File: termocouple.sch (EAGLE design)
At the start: 19 parts, among them IC1 MAX6675, IC2 MAX6675, IC3 MAX6675, IC4 MAX6675, U2 TC1262_VDB, X2 1751248, X3 1751248, X4 1751248, X5 1751248

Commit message: sch update
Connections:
- removed net 3V3: C4.1, U2.VOUT
- net +3V3: now also C4.1, U2.VOUT; no longer U$1.3.3V, U$1.3V3
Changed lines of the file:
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@@
 <part name="IC4" library="adafruit" deviceset="MAX6675" device=""/>
 <part name="+3V1" library="supply1" deviceset="+3V3" device=""/>
-<part name="+3V2" library="supply1" deviceset="+3V3" device=""/>
-<part name="+3V3" library="supply1" deviceset="+3V3" device=""/>
 <part name="GND1" library="supply1" deviceset="GND" device=""/>
 <part name="GND2" library="supply1" deviceset="GND" device=""/>
@@
 <part name="X4" library="con-phoenix-350" deviceset="1751248" device=""/>
 <part name="X5" library="con-phoenix-350" deviceset="1751248" device=""/>
+<part name="+3V6" library="supply1" deviceset="+3V3" device=""/>
 </parts>
 <sheets>
@@
 <instance part="IC4" gate="G$1" x="-5.08" y="22.86"/>
 <instance part="+3V1" gate="G$1" x="-25.4" y="78.74" rot="R90"/>
-<instance part="+3V2" gate="G$1" x="55.88" y="45.72" rot="R90"/>
-<instance part="+3V3" gate="G$1" x="99.06" y="58.42"/>
 <instance part="GND1" gate="1" x="86.36" y="81.28"/>
 <instance part="GND2" gate="1" x="-20.32" y="71.12" rot="R270"/>
@@
 <instance part="X5" gate="-1" x="-45.72" y="15.24" rot="R180"/>
 <instance part="X5" gate="-2" x="-45.72" y="25.4" rot="R180"/>
+<instance part="+3V6" gate="G$1" x="142.24" y="101.6"/>
 </instances>
 <busses>
@@
 </segment>
 <segment>
-<pinref part="U$1" gate="G$1" pin="3.3V"/>
-<pinref part="+3V2" gate="G$1" pin="+3V3"/>
-</segment>
-<segment>
-<pinref part="U$1" gate="G$1" pin="3V3"/>
-<pinref part="+3V3" gate="G$1" pin="+3V3"/>
-</segment>
-<segment>
 <pinref part="X1" gate="-1" pin="1"/>
 <pinref part="+3V4" gate="G$1" pin="+3V3"/>
+</segment>
+<segment>
+<pinref part="U2" gate="U1" pin="VOUT"/>
+<label x="139.7" y="101.6" size="1.778" layer="95"/>
+<pinref part="C4" gate="G$1" pin="1"/>
+<wire x1="137.16" y1="99.06" x2="142.24" y2="99.06" width="0.1524" layer="91"/>
+<wire x1="142.24" y1="99.06" x2="142.24" y2="96.52" width="0.1524" layer="91"/>
+<pinref part="+3V6" gate="G$1" pin="+3V3"/>
+<junction x="142.24" y="99.06"/>
 </segment>
 </net>
@@
 </segment>
 </net>
-<net name="3V3" class="0">
-<segment>
-<pinref part="U2" gate="U1" pin="VOUT"/>
-<label x="139.7" y="101.6" size="1.778" layer="95"/>
-<pinref part="C4" gate="G$1" pin="1"/>
-<wire x1="137.16" y1="99.06" x2="142.24" y2="99.06" width="0.1524" layer="91"/>
-<wire x1="142.24" y1="99.06" x2="142.24" y2="96.52" width="0.1524" layer="91"/>
-</segment>
-</net>

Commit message: pcb
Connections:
- net N$2: now also IC1.SCK
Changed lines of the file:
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@@
 <wire x1="104.14" y1="5.08" x2="20.32" y2="5.08" width="0.1524" layer="91"/>
 <wire x1="20.32" y1="5.08" x2="20.32" y2="20.32" width="0.1524" layer="91"/>
+<junction x="20.32" y="20.32"/>
 </segment>
 </net>
@@
 <wire x1="17.78" y1="38.1" x2="17.78" y2="60.96" width="0.1524" layer="91"/>
 <wire x1="17.78" y1="60.96" x2="17.78" y2="83.82" width="0.1524" layer="91"/>
-<wire x1="17.78" y1="83.82" x2="7.62" y2="83.82" width="0.1524" layer="91"/>
 <pinref part="IC3" gate="G$1" pin="SCK"/>
 <wire x1="10.16" y1="38.1" x2="17.78" y2="38.1" width="0.1524" layer="91"/>
@@
 <pinref part="U$1" gate="G$1" pin="D4"/>
 <wire x1="99.06" y1="25.4" x2="106.68" y2="25.4" width="0.1524" layer="91"/>
+<junction x="17.78" y="15.24"/>
+<pinref part="IC1" gate="G$1" pin="SCK"/>
+<wire x1="10.16" y1="83.82" x2="17.78" y2="83.82" width="0.1524" layer="91"/>
 </segment>
 </net>

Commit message: wiring change
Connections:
- removed net N$11: U$1.D11, X1-6.1
- removed net N$12: U$1.D12, X1-5.1
- new net N$24: X1-6.1
- new net N$25: X1-5.1
- net N$1: now also U$1.D7; no longer U$1.D3
- net N$10: no longer U$1.D10
- net N$2: now also U$1.D8; no longer U$1.D4
- net N$3: now also U$1.D10; no longer U$1.D6
- net N$4: now also U$1.D9; no longer U$1.D5
- net N$6: now also U$1.D11; no longer U$1.D7
- net N$7: now also U$1.D12; no longer U$1.D8
- net N$9: no longer U$1.D9
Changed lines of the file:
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@@
 <junction x="20.32" y="66.04"/>
 <junction x="20.32" y="43.18"/>
-<pinref part="U$1" gate="G$1" pin="D3"/>
-<wire x1="99.06" y1="22.86" x2="104.14" y2="22.86" width="0.1524" layer="91"/>
-<wire x1="104.14" y1="22.86" x2="104.14" y2="5.08" width="0.1524" layer="91"/>
+<wire x1="104.14" y1="33.02" x2="104.14" y2="5.08" width="0.1524" layer="91"/>
 <wire x1="104.14" y1="5.08" x2="20.32" y2="5.08" width="0.1524" layer="91"/>
 <wire x1="20.32" y1="5.08" x2="20.32" y2="20.32" width="0.1524" layer="91"/>
 <junction x="20.32" y="20.32"/>
+<pinref part="U$1" gate="G$1" pin="D7"/>
+<wire x1="99.06" y1="33.02" x2="104.14" y2="33.02" width="0.1524" layer="91"/>
 </segment>
 </net>
@@
 <wire x1="17.78" y1="15.24" x2="17.78" y2="2.54" width="0.1524" layer="91"/>
 <wire x1="17.78" y1="2.54" x2="106.68" y2="2.54" width="0.1524" layer="91"/>
-<wire x1="106.68" y1="2.54" x2="106.68" y2="25.4" width="0.1524" layer="91"/>
-<pinref part="U$1" gate="G$1" pin="D4"/>
-<wire x1="99.06" y1="25.4" x2="106.68" y2="25.4" width="0.1524" layer="91"/>
+<wire x1="106.68" y1="2.54" x2="106.68" y2="35.56" width="0.1524" layer="91"/>
 <junction x="17.78" y="15.24"/>
 <pinref part="IC1" gate="G$1" pin="SCK"/>
 <wire x1="10.16" y1="83.82" x2="17.78" y2="83.82" width="0.1524" layer="91"/>
+<pinref part="U$1" gate="G$1" pin="D8"/>
+<wire x1="99.06" y1="35.56" x2="106.68" y2="35.56" width="0.1524" layer="91"/>
 </segment>
 </net>
@@
 <wire x1="22.86" y1="86.36" x2="22.86" y2="0" width="0.1524" layer="91"/>
 <wire x1="22.86" y1="0" x2="109.22" y2="0" width="0.1524" layer="91"/>
-<wire x1="109.22" y1="0" x2="109.22" y2="27.94" width="0.1524" layer="91"/>
-<pinref part="U$1" gate="G$1" pin="D5"/>
-<wire x1="109.22" y1="27.94" x2="99.06" y2="27.94" width="0.1524" layer="91"/>
+<wire x1="109.22" y1="0" x2="109.22" y2="38.1" width="0.1524" layer="91"/>
+<pinref part="U$1" gate="G$1" pin="D9"/>
+<wire x1="99.06" y1="38.1" x2="109.22" y2="38.1" width="0.1524" layer="91"/>
 </segment>
 </net>
@@
 <pinref part="IC3" gate="G$1" pin="/CS"/>
 <wire x1="10.16" y1="40.64" x2="27.94" y2="40.64" width="0.1524" layer="91"/>
-<pinref part="U$1" gate="G$1" pin="D7"/>
-<wire x1="99.06" y1="33.02" x2="114.3" y2="33.02" width="0.1524" layer="91"/>
-<wire x1="114.3" y1="33.02" x2="114.3" y2="-5.08" width="0.1524" layer="91"/>
+<wire x1="114.3" y1="43.18" x2="114.3" y2="-5.08" width="0.1524" layer="91"/>
 <wire x1="114.3" y1="-5.08" x2="27.94" y2="-5.08" width="0.1524" layer="91"/>
 <wire x1="27.94" y1="-5.08" x2="27.94" y2="40.64" width="0.1524" layer="91"/>
-</segment>
-</net>
-<net name="N$3" class="0">
-<segment>
-<pinref part="IC2" gate="G$1" pin="/CS"/>
-<wire x1="10.16" y1="63.5" x2="25.4" y2="63.5" width="0.1524" layer="91"/>
-<wire x1="25.4" y1="63.5" x2="25.4" y2="-2.54" width="0.1524" layer="91"/>
-<pinref part="U$1" gate="G$1" pin="D6"/>
-<wire x1="111.76" y1="30.48" x2="99.06" y2="30.48" width="0.1524" layer="91"/>
-<wire x1="25.4" y1="-2.54" x2="111.76" y2="-2.54" width="0.1524" layer="91"/>
-<wire x1="111.76" y1="-2.54" x2="111.76" y2="30.48" width="0.1524" layer="91"/>
+<pinref part="U$1" gate="G$1" pin="D11"/>
+<wire x1="99.06" y1="43.18" x2="114.3" y2="43.18" width="0.1524" layer="91"/>
 </segment>
 </net>
@@
 <wire x1="15.24" y1="17.78" x2="15.24" y2="-7.62" width="0.1524" layer="91"/>
 <wire x1="15.24" y1="-7.62" x2="116.84" y2="-7.62" width="0.1524" layer="91"/>
-<wire x1="116.84" y1="-7.62" x2="116.84" y2="35.56" width="0.1524" layer="91"/>
-<pinref part="U$1" gate="G$1" pin="D8"/>
-<wire x1="116.84" y1="35.56" x2="99.06" y2="35.56" width="0.1524" layer="91"/>
+<wire x1="116.84" y1="-7.62" x2="116.84" y2="45.72" width="0.1524" layer="91"/>
+<pinref part="U$1" gate="G$1" pin="D12"/>
+<wire x1="116.84" y1="45.72" x2="99.06" y2="45.72" width="0.1524" layer="91"/>
 </segment>
 </net>
@@
 <net name="N$9" class="0">
 <segment>
-<pinref part="U$1" gate="G$1" pin="D9"/>
-<wire x1="99.06" y1="38.1" x2="121.92" y2="38.1" width="0.1524" layer="91"/>
-<wire x1="121.92" y1="38.1" x2="121.92" y2="27.94" width="0.1524" layer="91"/>
 <pinref part="X1" gate="-8" pin="1"/>
 <wire x1="121.92" y1="27.94" x2="152.4" y2="27.94" width="0.1524" layer="91"/>
@@
 <net name="N$10" class="0">
 <segment>
-<pinref part="U$1" gate="G$1" pin="D10"/>
-<wire x1="99.06" y1="40.64" x2="124.46" y2="40.64" width="0.1524" layer="91"/>
-<wire x1="124.46" y1="40.64" x2="124.46" y2="33.02" width="0.1524" layer="91"/>
 <pinref part="X1" gate="-7" pin="1"/>
 <wire x1="124.46" y1="33.02" x2="152.4" y2="33.02" width="0.1524" layer="91"/>
-</segment>
-</net>
-<net name="N$11" class="0">
-<segment>
-<pinref part="U$1" gate="G$1" pin="D11"/>
-<wire x1="99.06" y1="43.18" x2="127" y2="43.18" width="0.1524" layer="91"/>
-<wire x1="127" y1="43.18" x2="127" y2="38.1" width="0.1524" layer="91"/>
-<pinref part="X1" gate="-6" pin="1"/>
-<wire x1="127" y1="38.1" x2="152.4" y2="38.1" width="0.1524" layer="91"/>
-</segment>
-</net>
-<net name="N$12" class="0">
-<segment>
-<pinref part="U$1" gate="G$1" pin="D12"/>
-<wire x1="99.06" y1="45.72" x2="129.54" y2="45.72" width="0.1524" layer="91"/>
-<wire x1="129.54" y1="45.72" x2="129.54" y2="43.18" width="0.1524" layer="91"/>
-<pinref part="X1" gate="-5" pin="1"/>
-<wire x1="129.54" y1="43.18" x2="152.4" y2="43.18" width="0.1524" layer="91"/>
 </segment>
 </net>
@@
 </segment>
 </net>
+<net name="N$24" class="0">
+<segment>
+<pinref part="X1" gate="-6" pin="1"/>
+<wire x1="127" y1="38.1" x2="152.4" y2="38.1" width="0.1524" layer="91"/>
+</segment>
+</net>
+<net name="N$25" class="0">
+<segment>
+<pinref part="X1" gate="-5" pin="1"/>
+<wire x1="129.54" y1="43.18" x2="152.4" y2="43.18" width="0.1524" layer="91"/>
+</segment>
+</net>
+<net name="N$3" class="0">
+<segment>
+<pinref part="U$1" gate="G$1" pin="D10"/>
+<wire x1="99.06" y1="40.64" x2="111.76" y2="40.64" width="0.1524" layer="91"/>
+<pinref part="IC2" gate="G$1" pin="/CS"/>
+<wire x1="10.16" y1="63.5" x2="25.4" y2="63.5" width="0.1524" layer="91"/>
+<wire x1="25.4" y1="63.5" x2="25.4" y2="-2.54" width="0.1524" layer="91"/>
+<wire x1="25.4" y1="-2.54" x2="111.76" y2="-2.54" width="0.1524" layer="91"/>
+<wire x1="111.76" y1="-2.54" x2="111.76" y2="40.64" width="0.1524" layer="91"/>
+</segment>
+</net>

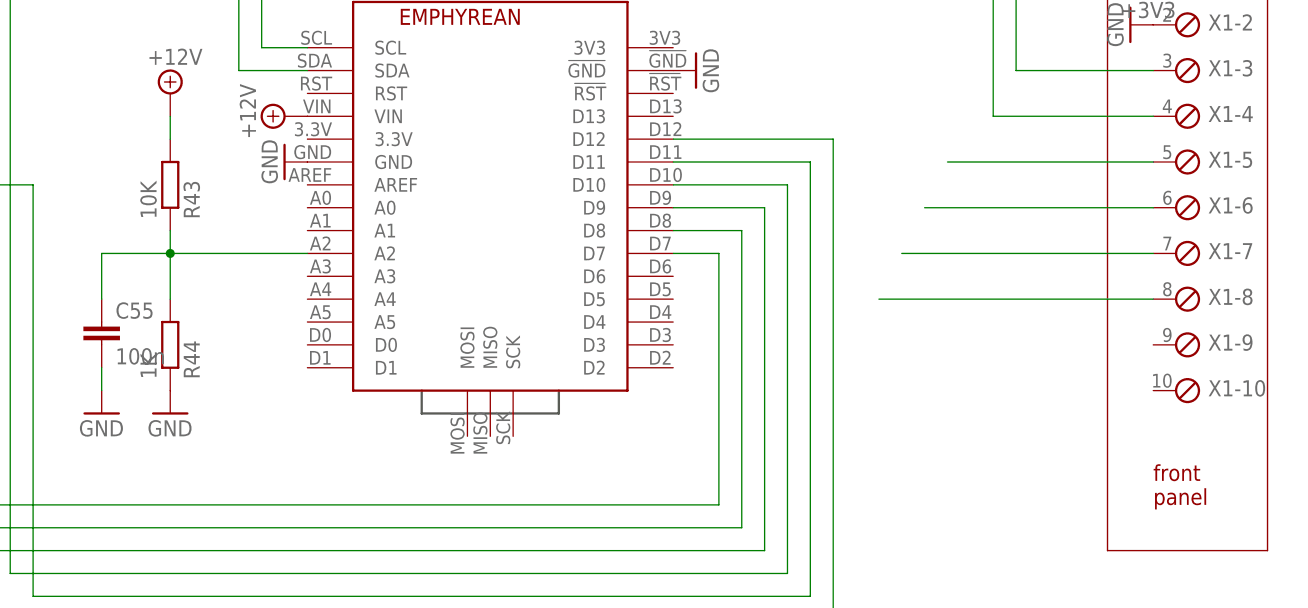
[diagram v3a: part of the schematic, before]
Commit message: front panel + brd traces
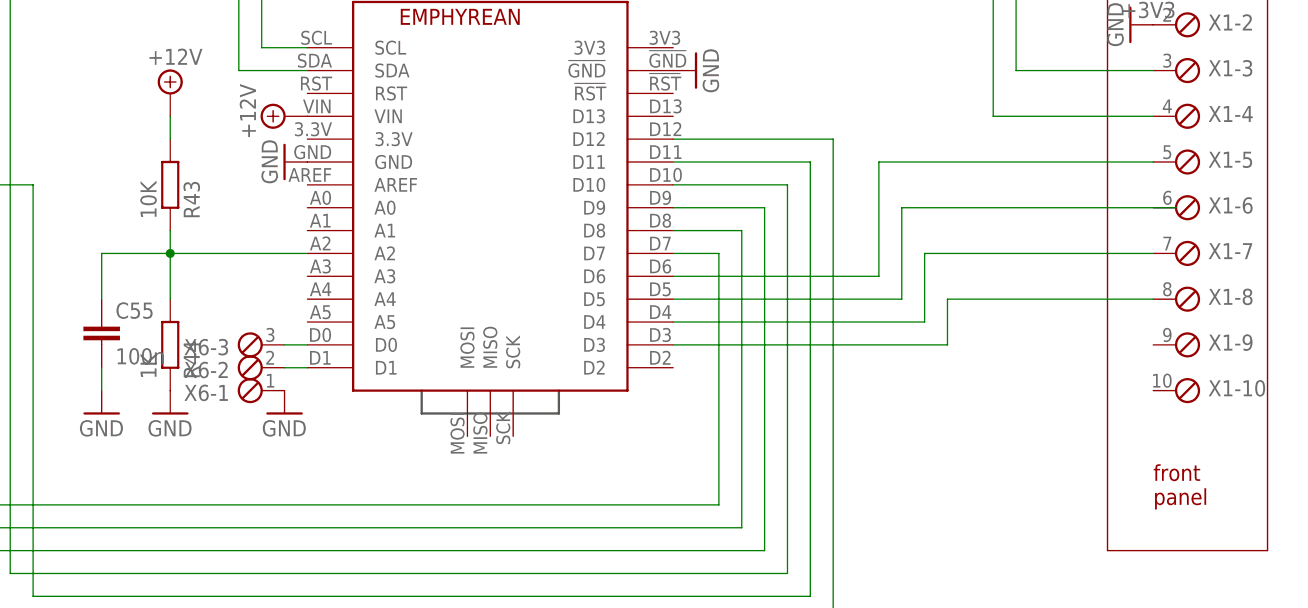
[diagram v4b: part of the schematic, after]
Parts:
- added X6: (no value), con-phoenix-254:MPT3
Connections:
- removed net N$24: X1-6.1
- removed net N$25: X1-5.1
- new net N$11: U$1.D4, X1-7.1
- new net N$12: U$1.D3, X1-8.1
- new net N$22: U$1.D0, X6-3.1
- new net N$23: U$1.D1, X6-2.1
- net GND: now also X6-1.1
- net N$10: now also U$1.D5; no longer X1-7.1
- net N$9: now also U$1.D6, X1-5.1; no longer X1-8.1
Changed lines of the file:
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@@
 <part name="X5" library="con-phoenix-350" deviceset="1751248" device=""/>
 <part name="+3V6" library="supply1" deviceset="+3V3" device=""/>
+<part name="X6" library="con-phoenix-254" deviceset="MPT3" device=""/>
+<part name="GND14" library="supply1" deviceset="GND" device=""/>
 </parts>
 <sheets>
@@
 <instance part="X5" gate="-2" x="-45.72" y="25.4" rot="R180"/>
 <instance part="+3V6" gate="G$1" x="142.24" y="101.6"/>
+<instance part="X6" gate="-1" x="53.34" y="17.78" rot="R180"/>
+<instance part="X6" gate="-2" x="53.34" y="20.32" rot="R180"/>
+<instance part="X6" gate="-3" x="53.34" y="22.86" rot="R180"/>
+<instance part="GND14" gate="1" x="55.88" y="15.24"/>
 </instances>
 <busses>
@@
 <junction x="48.26" y="93.98"/>
 </segment>
+<segment>
+<pinref part="X6" gate="-1" pin="1"/>
+<pinref part="GND14" gate="1" pin="GND"/>
+</segment>
 </net>
 <net name="N$4" class="0">
@@
 </segment>
 </net>
-<net name="N$9" class="0">
-<segment>
-<pinref part="X1" gate="-8" pin="1"/>
-<wire x1="121.92" y1="27.94" x2="152.4" y2="27.94" width="0.1524" layer="91"/>
-</segment>
-</net>
-<net name="N$10" class="0">
-<segment>
-<pinref part="X1" gate="-7" pin="1"/>
-<wire x1="124.46" y1="33.02" x2="152.4" y2="33.02" width="0.1524" layer="91"/>
-</segment>
-</net>
 <net name="N$13" class="0">
 <segment>
@@
 <wire x1="-17.78" y1="88.9" x2="-43.18" y2="88.9" width="0.1524" layer="91"/>
 <wire x1="-43.18" y1="88.9" x2="-43.18" y2="91.44" width="0.1524" layer="91"/>
-</segment>
-</net>
-<net name="N$24" class="0">
-<segment>
-<pinref part="X1" gate="-6" pin="1"/>
-<wire x1="127" y1="38.1" x2="152.4" y2="38.1" width="0.1524" layer="91"/>
-</segment>
-</net>
-<net name="N$25" class="0">
-<segment>
-<pinref part="X1" gate="-5" pin="1"/>
-<wire x1="129.54" y1="43.18" x2="152.4" y2="43.18" width="0.1524" layer="91"/>
 </segment>
 </net>
@@
 </segment>
 </net>
+<net name="N$9" class="0">
+<segment>
+<pinref part="U$1" gate="G$1" pin="D6"/>
+<wire x1="99.06" y1="30.48" x2="121.92" y2="30.48" width="0.1524" layer="91"/>
+<wire x1="121.92" y1="30.48" x2="121.92" y2="43.18" width="0.1524" layer="91"/>
+<pinref part="X1" gate="-5" pin="1"/>
+<wire x1="121.92" y1="43.18" x2="152.4" y2="43.18" width="0.1524" layer="91"/>
+</segment>
+</net>
+<net name="N$10" class="0">
+<segment>
+<wire x1="154.94" y1="38.1" x2="124.46" y2="38.1" width="0.1524" layer="91"/>
+<wire x1="124.46" y1="38.1" x2="124.46" y2="27.94" width="0.1524" layer="91"/>
+<pinref part="U$1" gate="G$1" pin="D5"/>
+<wire x1="124.46" y1="27.94" x2="99.06" y2="27.94" width="0.1524" layer="91"/>
+</segment>
+</net>
+<net name="N$11" class="0">
+<segment>
+<pinref part="U$1" gate="G$1" pin="D4"/>
+<wire x1="99.06" y1="25.4" x2="127" y2="25.4" width="0.1524" layer="91"/>
+<wire x1="127" y1="25.4" x2="127" y2="33.02" width="0.1524" layer="91"/>
+<pinref part="X1" gate="-7" pin="1"/>
+<wire x1="127" y1="33.02" x2="152.4" y2="33.02" width="0.1524" layer="91"/>
+</segment>
+</net>
+<net name="N$12" class="0">
+<segment>
+<pinref part="U$1" gate="G$1" pin="D3"/>
+<wire x1="99.06" y1="22.86" x2="129.54" y2="22.86" width="0.1524" layer="91"/>
+<wire x1="129.54" y1="22.86" x2="129.54" y2="27.94" width="0.1524" layer="91"/>
+<pinref part="X1" gate="-8" pin="1"/>
+<wire x1="129.54" y1="27.94" x2="152.4" y2="27.94" width="0.1524" layer="91"/>
+</segment>
+</net>
+<net name="N$22" class="0">
+<segment>
+<pinref part="U$1" gate="G$1" pin="D0"/>
+<pinref part="X6" gate="-3" pin="1"/>
+<wire x1="55.88" y1="22.86" x2="58.42" y2="22.86" width="0.1524" layer="91"/>
+</segment>
+</net>
+<net name="N$23" class="0">
+<segment>
+<pinref part="U$1" gate="G$1" pin="D1"/>
+<pinref part="X6" gate="-2" pin="1"/>
+<wire x1="55.88" y1="20.32" x2="58.42" y2="20.32" width="0.1524" layer="91"/>
+</segment>
+</net>

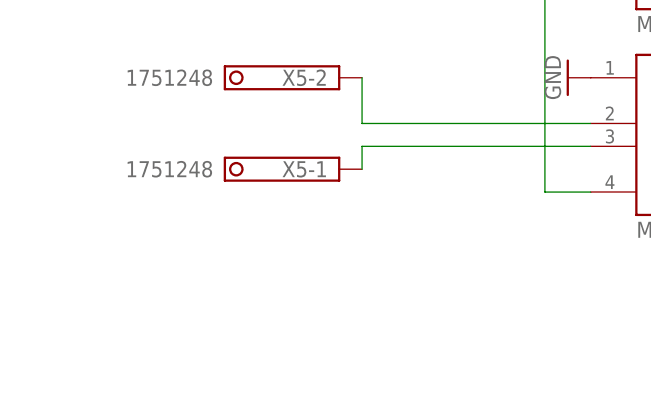
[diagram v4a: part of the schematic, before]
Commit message: BRD added thermocouple device
thermocouple
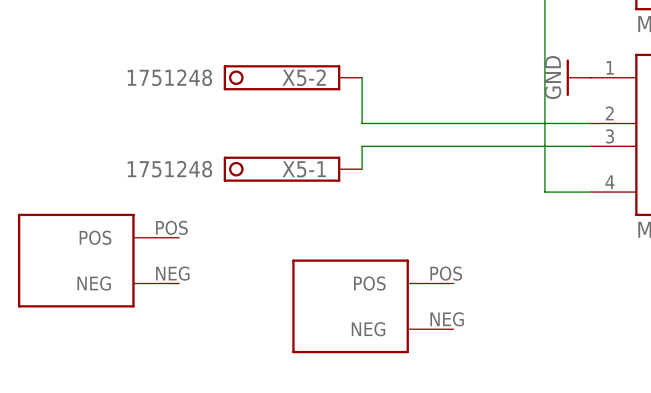
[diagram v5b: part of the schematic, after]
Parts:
- added U$2, U$3: THERMOCOUPLE, mine:THERMOCOUPLE
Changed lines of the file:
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@@
 <part name="X6" library="con-phoenix-254" deviceset="MPT3" device=""/>
 <part name="GND14" library="supply1" deviceset="GND" device=""/>
+<part name="U$2" library="mine" deviceset="THERMOCOUPLE" device=""/>
+<part name="U$3" library="mine" deviceset="THERMOCOUPLE" device=""/>
 </parts>
 <sheets>
@@
 <instance part="X6" gate="-3" x="53.34" y="22.86" rot="R180"/>
 <instance part="GND14" gate="1" x="55.88" y="15.24"/>
+<instance part="U$2" gate="G$1" x="-38.1" y="-7.62" rot="MR0"/>
+<instance part="U$3" gate="G$1" x="-68.58" y="-2.54" rot="MR0"/>
 </instances>
 <busses>
